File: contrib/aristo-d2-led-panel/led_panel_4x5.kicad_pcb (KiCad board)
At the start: 4 copper layers, 153.5 x 153.5 mm, 230 parts, among them U10 C5348912_LED-SMD_4P-L5.0-W4.9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, U101 C5348912_LED-SMD_4P-L5.0-W4.9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, U103 C5348912_LED-SMD_4P-L5.0-W4.9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, U105 C5348912_LED-SMD_4P-L5.0-W4.9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, U107 C5348912_LED-SMD_4P-L5.0-W4.9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, U109 C5348912_LED-SMD_4P-L5.0-W4.9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, U111 C5348912_LED-SMD_4P-L5.0-W4.9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, U113 C5348912_LED-SMD_4P-L5.0-W4.9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, U115 C5348912_LED-SMD_4P-L5.0-W4.9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, U117 C5348912_LED-SMD_4P-L5.0-W4.9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, U119 C5348912_LED-SMD_4P-L5.0-W4.9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, U121 C5348912_LED-SMD_4P-L5.0-W4.9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, U123 C5348912_LED-SMD_4P-L5.0-W4.9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, U125 C5348912_LED-SMD_4P-L5.0-W4.9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, U127 C5348912_LED-SMD_4P-L5.0-W4.9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, U129 C5348912_LED-SMD_4P-L5.0-W4.9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, U13 C5348912_LED-SMD_4P-L5.0-W4.9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, U131 C5348912_LED-SMD_4P-L5.0-W4.9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, U133 C5348912_LED-SMD_4P-L5.0-W4.9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, U135 C5348912_LED-SMD_4P-L5.0-W4.9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, U137 C5348912_LED-SMD_4P-L5.0-W4.9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, U139 C5348912_LED-SMD_4P-L5.0-W4.9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, U141 C5348912_LED-SMD_4P-L5.0-W4.9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, U143 C5348912_LED-SMD_4P-L5.0-W4.9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, U145 C5348912_LED-SMD_4P-L5.0-W4.9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, U147 C5348912_LED-SMD_4P-L5.0-W4.9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, U149 C5348912_LED-SMD_4P-L5.0-W4.9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, U15 C5348912_LED-SMD_4P-L5.0-W4.9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, U151 C5348912_LED-SMD_4P-L5.0-W4.9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, U153 C5348912_LED-SMD_4P-L5.0-W4.9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, U155 C5348912_LED-SMD_4P-L5.0-W4.9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, U157 C5348912_LED-SMD_4P-L5.0-W4.9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, U159 C5348912_LED-SMD_4P-L5.0-W4.9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, U162 C5348912_LED-SMD_4P-L5.0-W4.9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, U164 C5348912_LED-SMD_4P-L5.0-W4.9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, U166 C5348912_LED-SMD_4P-L5.0-W4.9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, U168 C5348912_LED-SMD_4P-L5.0-W4.9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, U17 C5348912_LED-SMD_4P-L5.0-W4.9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, U170 C5348912_LED-SMD_4P-L5.0-W4.9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, U172 C5348912_LED-SMD_4P-L5.0-W4.9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, U174 C5348912_LED-SMD_4P-L5.0-W4.9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, U176 C5348912_LED-SMD_4P-L5.0-W4.9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, U178 C5348912_LED-SMD_4P-L5.0-W4.9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, U181 C5348912_LED-SMD_4P-L5.0-W4.9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, U183 C5348912_LED-SMD_4P-L5.0-W4.9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, U185 C5348912_LED-SMD_4P-L5.0-W4.9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, U187 C5348912_LED-SMD_4P-L5.0-W4.9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, U189 C5348912_LED-SMD_4P-L5.0-W4.9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, U19 C5348912_LED-SMD_4P-L5.0-W4.9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, U191 C5348912_LED-SMD_4P-L5.0-W4.9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, U193 C5348912_LED-SMD_4P-L5.0-W4.9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, U195 C5348912_LED-SMD_4P-L5.0-W4.9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, U197 C5348912_LED-SMD_4P-L5.0-W4.9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, U2 C5348912_LED-SMD_4P-L5.0-W4.9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, U200 C5348912_LED-SMD_4P-L5.0-W4.9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, U202 C5348912_LED-SMD_4P-L5.0-W4.9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, U204 C5348912_LED-SMD_4P-L5.0-W4.9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, U206 C5348912_LED-SMD_4P-L5.0-W4.9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, U208 C5348912_LED-SMD_4P-L5.0-W4.9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, U21 C5348912_LED-SMD_4P-L5.0-W4.9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, U218 C5348912_LED-SMD_4P-L5.0-W4.9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, U219 C5348912_LED-SMD_4P-L5.0-W4.9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, U220 C5348912_LED-SMD_4P-L5.0-W4.9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, U221 C5348912_LED-SMD_4P-L5.0-W4.9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, U222 C5348912_LED-SMD_4P-L5.0-W4.9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, U223 C5348912_LED-SMD_4P-L5.0-W4.9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, U224 C5348912_LED-SMD_4P-L5.0-W4.9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, U225 C5348912_LED-SMD_4P-L5.0-W4.9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, U226 C7484_SOT-23-5_L3.0-W1.7-P0.9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, U23 C5348912_LED-SMD_4P-L5.0-W4.9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, U25 C5348912_LED-SMD_4P-L5.0-W4.9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, U27 C5348912_LED-SMD_4P-L5.0-W4.9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, U29 C5348912_LED-SMD_4P-L5.0-W4.9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, U32 C5348912_LED-SMD_4P-L5.0-W4.9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, U34 C5348912_LED-SMD_4P-L5.0-W4.9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, U36 C5348912_LED-SMD_4P-L5.0-W4.9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, U38 C5348912_LED-SMD_4P-L5.0-W4.9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, U4 C5348912_LED-SMD_4P-L5.0-W4.9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, U40 C5348912_LED-SMD_4P-L5.0-W4.9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, U42 C5348912_LED-SMD_4P-L5.0-W4.9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

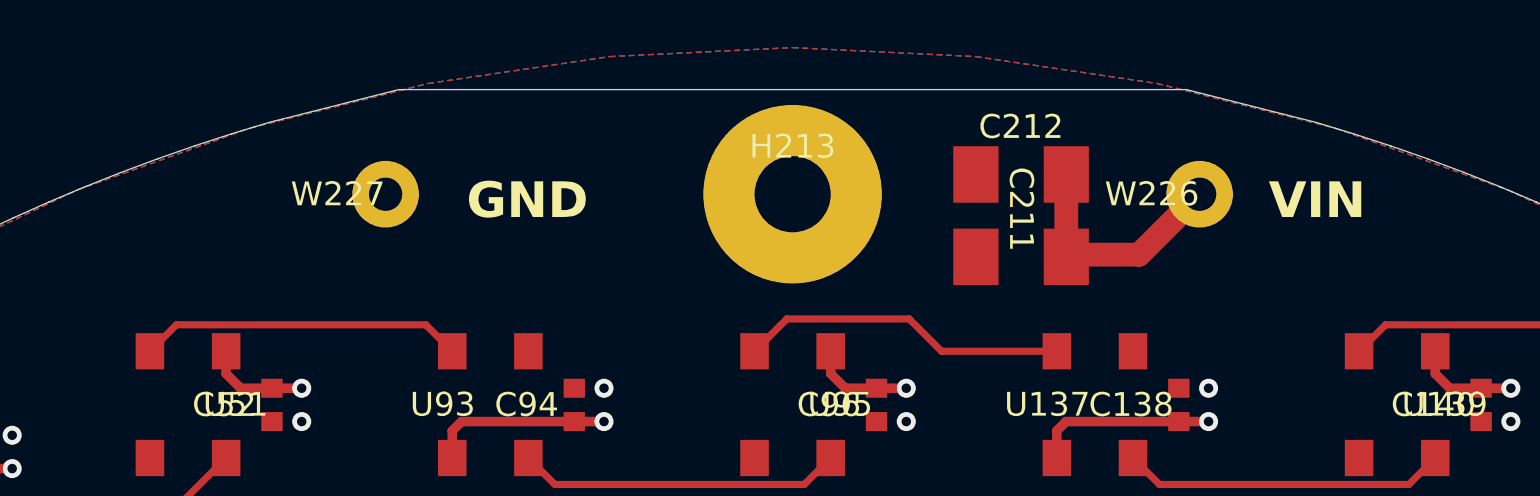
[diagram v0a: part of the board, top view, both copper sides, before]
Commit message: Publish the production Aristo D2 board with the power pads shifted 0.75 mm.
JLCPCB DFM flagged THT-to-SMD clearance at the 5V/GND wire pads; the new Gerbers clear that without moving the LEDs.

Co-authored-by: Cursor <cursoragent@cursor.com>
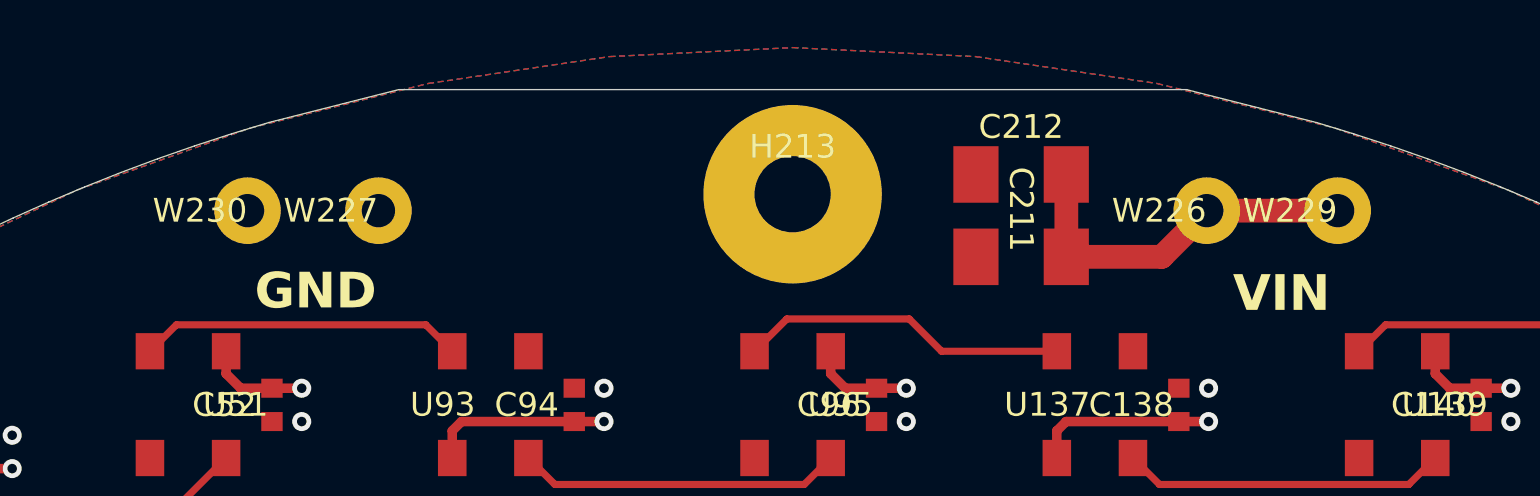
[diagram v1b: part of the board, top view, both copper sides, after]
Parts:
- added W229: WirePad_PTH_2.8_1.4, jlcpcb_parts:WirePad_PTH_2.8_1.4, F.Cu at (171.4, 33.4)
- added W230: WirePad_PTH_2.8_1.4, jlcpcb_parts:WirePad_PTH_2.8_1.4, F.Cu at (125.6, 33.4)
- moved W226 0.75 mm to (165.9, 33.4)
- moved W227 0.75 mm to (131.1, 33.4)
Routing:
- net 5V: track 657.7 -> 663.4 mm
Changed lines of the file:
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@@
 		(embedded_fonts no)
 	)
+	(footprint "jlcpcb_parts:WirePad_PTH_2.8_1.4"
+		(layer "F.Cu")
+		(at 125.6 33.35 90)
+		(property "Reference" "W230"
+			(at 0 -2 0)
+			(unlocked yes)
+			(layer "F.SilkS")
+			(effects
+				(font
+					(size 1 1)
+					(line_spacing 0)
+					(thickness 0.15)
+				)
+			)
+		)
+		(property "Value" "WirePad_PTH_2.8_1.4"
+			(at 0 2 0)
+			(unlocked yes)
+			(layer "F.Fab")
+			(effects
+				(font
+					(size 1 1)
+					(line_spacing 0)
+					(thickness 0.15)
+				)
+			)
+		)
+		(property "Datasheet" ""
+			(at -0.75 0 90)
+			(layer "F.Fab")
+			(hide yes)
+			(effects
+				(font
+					(size 1.27 1.27)
+				)
+			)
+		)
+		(property "Description" ""
+			(at -0.75 0 90)
+			(layer "F.Fab")
+			(hide yes)
+			(effects
+				(font
+					(size 1.27 1.27)
+				)
+			)
+		)
+		(duplicate_pad_numbers_are_jumpers no)
+		(pad "1" thru_hole circle
+			(at 0 0 90)
+			(size 2.8 2.8)
+			(drill 1.4)
+			(layers "*.Cu" "*.Mask")
+			(remove_unused_layers no)
+			(net "GND")
+			(padstack
+				(mode front_inner_back)
+				(layer "Inner"
+					(shape circle)
+					(size 2.8 2.8)
+				)
+				(layer "B.Cu"
+					(shape circle)
+					(size 2.8 2.8)
+				)
+			)
+		)
+		(embedded_fonts no)
+	)
 	(footprint "jlcpcb_parts:C14663_C0603"
 		(layer "F.Cu")
@@
 		(embedded_fonts no)
 	)
+	(footprint "jlcpcb_parts:WirePad_PTH_2.8_1.4"
+		(layer "F.Cu")
+		(at 171.4 33.35 90)
+		(property "Reference" "W229"
+			(at 0 -2 0)
+			(unlocked yes)
+			(layer "F.SilkS")
+			(effects
+				(font
+					(size 1 1)
+					(line_spacing 0)
+					(thickness 0.15)
+				)
+			)
+		)
+		(property "Value" "WirePad_PTH_2.8_1.4"
+			(at 0 2 0)
+			(unlocked yes)
+			(layer "F.Fab")
+			(effects
+				(font
+					(size 1 1)
+					(line_spacing 0)
+					(thickness 0.15)
+				)
+			)
+		)
+		(property "Datasheet" ""
+			(at -0.75 0 90)
+			(layer "F.Fab")
+			(hide yes)
+			(effects
+				(font
+					(size 1.27 1.27)
+				)
+			)
+		)
+		(property "Description" ""
+			(at -0.75 0 90)
+			(layer "F.Fab")
+			(hide yes)
+			(effects
+				(font
+					(size 1.27 1.27)
+				)
+			)
+		)
+		(duplicate_pad_numbers_are_jumpers no)
+		(pad "1" thru_hole circle
+			(at 0 0 90)
+			(size 2.8 2.8)
+			(drill 1.4)
+			(layers "*.Cu" "*.Mask")
+			(remove_unused_layers no)
+			(net "5V")
+			(padstack
+				(mode front_inner_back)
+				(layer "Inner"
+					(shape circle)
+					(size 2.8 2.8)
+				)
+				(layer "B.Cu"
+					(shape circle)
+					(size 2.8 2.8)
+				)
+			)
+		)
+		(embedded_fonts no)
+	)
 	(footprint "jlcpcb_parts:C14663_C0603"
 		(layer "F.Cu")
@@
 	(footprint "jlcpcb_parts:WirePad_PTH_2.8_1.4"
 		(layer "F.Cu")
-		(at 131.4 32.66 90)
+		(at 131.1 33.35 90)
 		(property "Reference" "W227"
 			(at 0 -2 0)
@@
 		)
 		(property "Datasheet" ""
-			(at 0 0 90)
+			(at -0.75 0.3 90)
 			(layer "F.Fab")
 			(hide yes)
@@
 		)
 		(property "Description" ""
-			(at 0 0 90)
+			(at -0.75 0.3 90)
 			(layer "F.Fab")
 			(hide yes)
@@
 	(footprint "jlcpcb_parts:WirePad_PTH_2.8_1.4"
 		(layer "F.Cu")
-		(at 165.6 32.66 90)
+		(at 165.9 33.35 90)
 		(property "Reference" "W226"
 			(at 0 -2 0)
@@
 		)
 		(property "Datasheet" ""
-			(at 0 0 90)
+			(at -0.75 0 90)
 			(layer "F.Fab")
 			(hide yes)
@@
 		)
 		(property "Description" ""
-			(at 0 0 90)
+			(at -0.75 0 90)
 			(layer "F.Fab")
 			(hide yes)
@@
 	)
 	(gr_text "GND"
-		(at 134.8 33.8 0)
+		(at 125.9 37.6 0)
 		(layer "F.SilkS")
 		(effects
@@
 		)
 	)
-	(gr_text "DATA"
-		(at 167.9 178.4 0)
+	(gr_text "VIN"
+		(at 167 37.7 0)
 		(layer "F.SilkS")
 		(effects
@@
 		)
 	)
-	(gr_text "VIN"
-		(at 168.5 33.8 0)
+	(gr_text "DATA"
+		(at 167.9 178.4 0)
 		(layer "F.SilkS")
 		(effects
@@
 	)
 	(segment
-		(start 163.06 35.2)
-		(end 160.0886 35.2)
-		(width 1)
-		(layer "F.Cu")
-		(net "5V")
-	)
-	(segment
 		(start 109.189 131.111)
 		(end 113.926 131.111)
@@
 	)
 	(segment
-		(start 165.6 32.66)
-		(end 163.06 35.2)
-		(width 1)
-		(layer "F.Cu")
-		(net "5V")
-	)
-	(segment
 		(start 159.6001 144.1999)
 		(end 159.989 143.811)
@@
 	)
 	(segment
+		(start 159.9986 35.29)
+		(end 164.01 35.29)
+		(width 1)
+		(layer "F.Cu")
+		(net "5V")
+	)
+	(segment
 		(start 124.6999 167.1999)
 		(end 125.311 167.811)
@@
 	)
 	(segment
+		(start 165.9 33.35)
+		(end 171.4 33.35)
+		(width 1)
+		(layer "F.Cu")
+		(net "5V")
+	)
+	(segment
 		(start 84.1261 71.1783)
 		(end 84.1261 70.0359)
@@
 	)
 	(segment
+		(start 165.9 33.4)
+		(end 165.9 33.35)
+		(width 1)
+		(layer "F.Cu")
+		(net "5V")
+	)
+	(segment
 		(start 134.2001 67.9999)
 		(end 134.589 67.611)
@@
 	)
 	(segment
+		(start 164.01 35.29)
+		(end 165.9 33.4)
+		(width 1)
+		(layer "F.Cu")
+		(net "5V")
+	)
+	(segment
 		(start 159.6001 43.7423)
 		(end 159.6001 42.5999)
@@
 	)
 	(segment
+		(start 159.3 178.7)
+		(end 158.1 177.5)
+		(width 0.3)
+		(layer "F.Cu")
+		(net "DATA_IN")
+	)
+	(segment
+		(start 158.1 177.5)
+		(end 158.1 175.9)
+		(width 0.3)
+		(layer "F.Cu")
+		(net "DATA_IN")
+	)
+	(segment
+		(start 159.3 179.1999)
+		(end 159.3 178.7)
+		(width 0.3)
+		(layer "F.Cu")
+		(net "DATA_IN")
+	)
+	(segment
+		(start 159.2999 179.2)
+		(end 163.09 179.2)
+		(width 0.3)
+		(layer "F.Cu")
+		(net "DATA_IN")
+	)
+	(segment
+		(start 158.1 175.9)
+		(end 158.59 175.41)
+		(width 0.3)
+		(layer "F.Cu")
+		(net "DATA_IN")
+	)
+	(segment
+		(start 158.59 175.41)
+		(end 159.4001 175.41)
+		(width 0.3)
+		(layer "F.Cu")
+		(net "DATA_IN")
+	)
+	(segment
+		(start 159.2999 179.2)
+		(end 159.3 179.1999)
+		(width 0.3)
+		(layer "F.Cu")
+		(net "DATA_IN")
+	)
+	(segment
+		(start 163.09 179.2)
+		(end 164.95 177.34)
+		(width 0.3)
+		(layer "F.Cu")
+		(net "DATA_IN")
+	)
+	(segment
 		(start 202.0121 108.3543)
 		(end 200.8999 107.2421)
@@
 	)
 	(segment
-		(start 159.3 178.7)
-		(end 158.1 177.5)
-		(width 0.3)
-		(layer "F.Cu")
-		(net "DATA_IN")
-	)
-	(segment
-		(start 158.1 177.5)
-		(end 158.1 175.9)
-		(width 0.3)
-		(layer "F.Cu")
-		(net "DATA_IN")
-	)
-	(segment
-		(start 159.3 179.1999)
-		(end 159.3 178.7)
-		(width 0.3)
-		(layer "F.Cu")
-		(net "DATA_IN")
-	)
-	(segment
-		(start 159.2999 179.2)
-		(end 163.09 179.2)
-		(width 0.3)
-		(layer "F.Cu")
-		(net "DATA_IN")
-	)
-	(segment
-		(start 158.1 175.9)
-		(end 158.59 175.41)
-		(width 0.3)
-		(layer "F.Cu")
-		(net "DATA_IN")
-	)
-	(segment
-		(start 158.59 175.41)
-		(end 159.4001 175.41)
-		(width 0.3)
-		(layer "F.Cu")
-		(net "DATA_IN")
-	)
-	(segment
-		(start 159.2999 179.2)
-		(end 159.3 179.1999)
-		(width 0.3)
-		(layer "F.Cu")
-		(net "DATA_IN")
-	)
-	(segment
-		(start 163.09 179.2)
-		(end 164.95 177.34)
-		(width 0.3)
-		(layer "F.Cu")
-		(net "DATA_IN")
-	)
-	(segment
 		(start 162.7999 170.7421)
 		(end 163.9119 171.8541)
@@
 		(layer "F.Cu")
 		(name "GND_F")
-		(hatch edge 0)
+		(hatch edge 0.1)
 		(connect_pads
 			(clearance 0.2)
@@
 		(layer "B.Cu")
 		(name "GND_B")
-		(hatch edge 0)
+		(hatch edge 0.1)
 		(connect_pads thru_hole_only
 			(clearance 0.2)
@@
 		(layer "In1.Cu")
 		(name "5V_IN1")
-		(hatch edge 0)
+		(hatch edge 0.1)
 		(connect_pads thru_hole_only
 			(clearance 0.2)
@@
 		(layer "In2.Cu")
 		(name "GND_IN2")
-		(hatch edge 0)
+		(hatch edge 0.1)
 		(connect_pads thru_hole_only
 			(clearance 0.2)

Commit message: Publish the Aristo D2 gerbers that were sent to JLCPCB.
The ordered set matches copper, BOM and CPL already on main; this adds the backside load table from the 31 Aug export.

Co-authored-by: Cursor <cursoragent@cursor.com>
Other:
- board text added: "5V + ESP32"
- board text added: "FOCUS W 2.3A 12W"
- board text added: "MAX RGBW 5.0A 25W"
- board text added: "SPLIT G+B 2.3A 12W"
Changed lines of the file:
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@@
+		)
+	)
+	(gr_text "FOCUS W  2.3A  12W"
+		(at 148.5 45.23 0)
+		(layer "B.SilkS")
+		(effects
+			(font
+				(size 1.4 1.4)
+				(thickness 0.21)
+			)
+			(justify mirror)
+		)
+	)
+	(gr_text "SPLIT G+B  2.3A  12W"
+		(at 148.5 46.98 0)
+		(layer "B.SilkS")
+		(effects
+			(font
+				(size 1.4 1.4)
+				(thickness 0.21)
+			)
+			(justify mirror)
+		)
+	)
+	(gr_text "MAX RGBW  5.0A  25W"
+		(at 148.5 48.73 0)
+		(layer "B.SilkS")
+		(effects
+			(font
+				(size 1.4 1.4)
+				(thickness 0.21)
+			)
+			(justify mirror)
+		)
+	)
+	(gr_text "5V + ESP32"
+		(at 148.5 50.48 0)
+		(layer "B.SilkS")
+		(effects
+			(font
+				(size 1.4 1.4)
+				(thickness 0.21)
+			)
+			(justify mirror)
 		)
 	)
